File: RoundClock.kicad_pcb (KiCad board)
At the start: 2 copper layers, 100 x 100 mm, 359 parts, among them J101 Jack-DC, J1101 UART, J1102 USB_OTG, J902 I2C, J904 ISP, SW301 SW_Push, SW302 SW_Push, SW303 SW_Push, SW304 SW_Push, SW305 SW_Push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

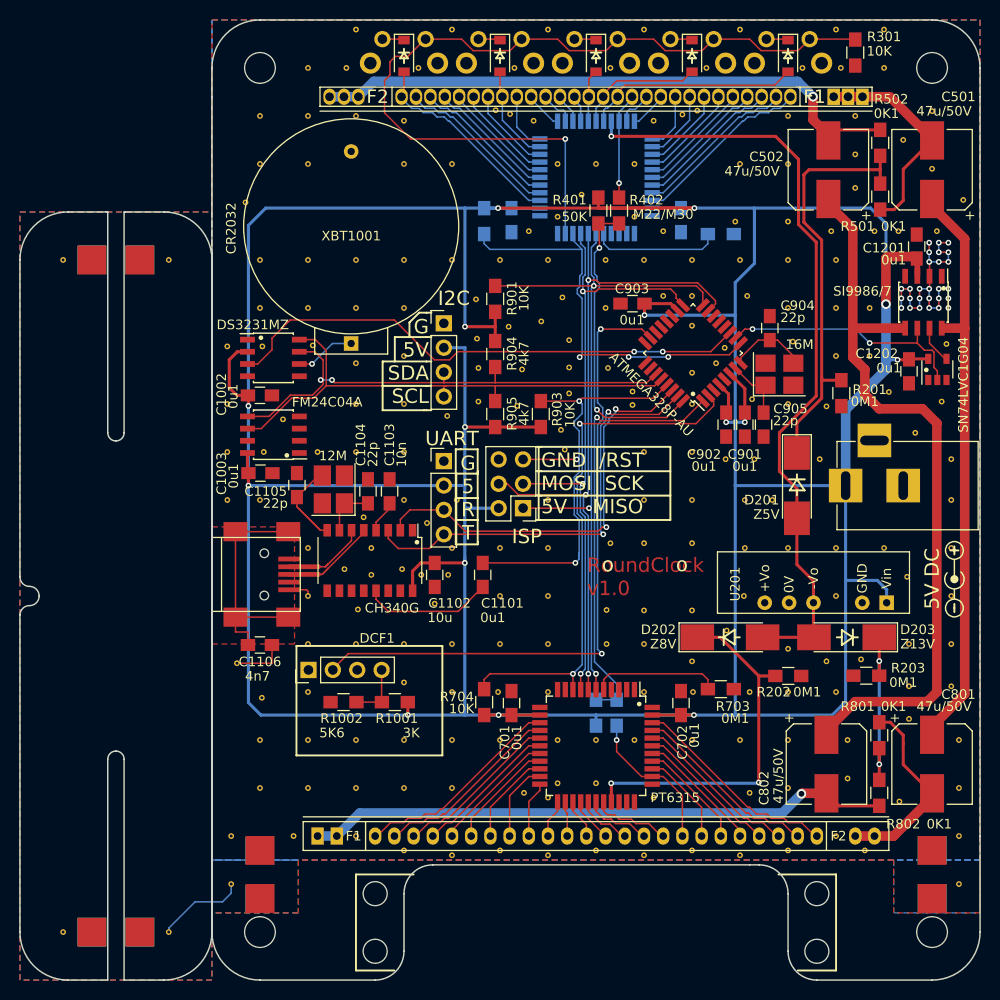
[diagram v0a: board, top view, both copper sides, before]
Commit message: switching to more convenient notation of values, e.g. 100K instead of 0M1
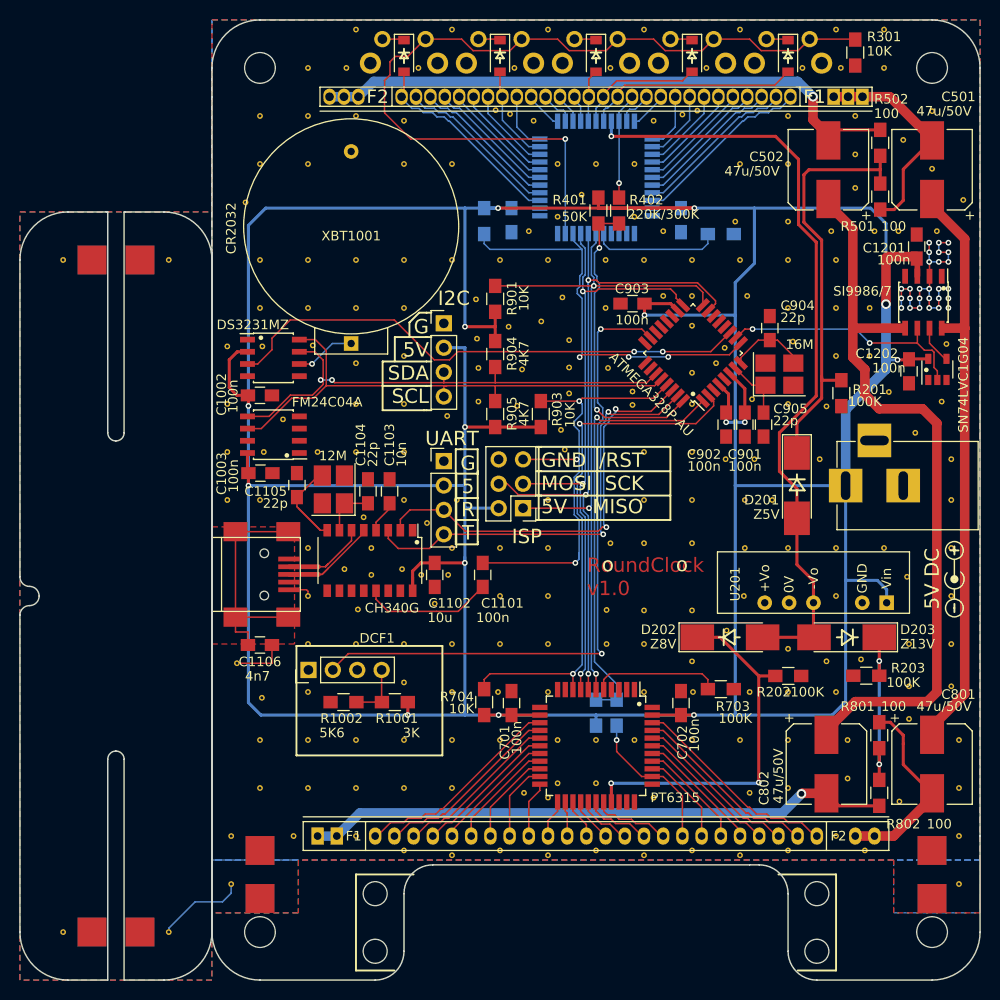
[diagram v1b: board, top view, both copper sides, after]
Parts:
- C1002, C1003, C1101, C1201, C1202, C401, C402, C701, C702, C901, C902, C903: value 0u1 -> 100n
- R201, R202, R203, R403, R703: value 0M1 -> 100K
- R402, R702: value M22/M30 -> 220K/300K
- R501, R502, R801, R802: value 0K1 -> 100
- R904, R905: value 4k7 -> 4K7
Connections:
- J1102 pad 1: (no net) -> Net-(J1102-Pad1)
- J1102 pad 4: (no net) -> Net-(J1102-Pad4)
- U1002 pad 1: (no net) -> Net-(U1002-Pad1)
- U1002 pad 4: (no net) -> Net-(U1002-Pad4)
- U1003 pad 1: (no net) -> Net-(U1003-Pad1)
- U1003 pad 2: (no net) -> Net-(U1003-Pad2)
- U1003 pad 3: (no net) -> Net-(U1003-Pad3)
- U1003 pad 7: (no net) -> Net-(U1003-Pad7)
- U1103 pad 10: (no net) -> Net-(U1103-Pad10)
- U1103 pad 11: (no net) -> Net-(U1103-Pad11)
- U1103 pad 12: (no net) -> Net-(U1103-Pad12)
- U1103 pad 14: (no net) -> Net-(U1103-Pad14)
- U1103 pad 15: (no net) -> Net-(U1103-Pad15)
- U1103 pad 9: (no net) -> Net-(U1103-Pad9)
- U1201 pad 1: (no net) -> Net-(U1201-Pad1)
- U201 pad 5: (no net) -> Net-(U201-Pad5)
- U401 pad 1: (no net) -> Net-(U401-Pad1)
- U401 pad 11: (no net) -> Net-(U401-Pad11)
- U401 pad 2: (no net) -> Net-(U401-Pad2)
- U401 pad 3: (no net) -> Net-(U401-Pad3)
- U401 pad 4: (no net) -> Net-(U401-Pad4)
- U701 pad 1: (no net) -> Net-(U701-Pad1)
- U701 pad 10: (no net) -> /TextDisplay/DisplayCtrlText/K
- U701 pad 11: (no net) -> Net-(U701-Pad11)
- U701 pad 2: (no net) -> Net-(U701-Pad2)
- U701 pad 3: (no net) -> Net-(U701-Pad3)
- U701 pad 31: (no net) -> /TextDisplay/DisplayCtrlText/G12
- U701 pad 32: (no net) -> /TextDisplay/DisplayCtrlText/G11
- U701 pad 33: (no net) -> /TextDisplay/DisplayCtrlText/G10
- U701 pad 34: (no net) -> /TextDisplay/DisplayCtrlText/G9
- U701 pad 4: (no net) -> Net-(U701-Pad4)
- U901 pad 12: (no net) -> Net-(U901-Pad12)
- U901 pad 13: (no net) -> Net-(U901-Pad13)
- U901 pad 14: (no net) -> Net-(U901-Pad14)
- U901 pad 19: (no net) -> Net-(U901-Pad19)
- U901 pad 20: (no net) -> Net-(U901-Pad20)
- U901 pad 22: (no net) -> Net-(U901-Pad22)
- U901 pad 24: (no net) -> Net-(U901-Pad24)
- U901 pad 25: (no net) -> Net-(U901-Pad25)
- U901 pad 26: (no net) -> Net-(U901-Pad26)
